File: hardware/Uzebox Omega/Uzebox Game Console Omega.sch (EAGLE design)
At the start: 82 parts, among them CON1 USBSERIALSMD, IC1 MCP1700, IC2 7805T, J1 MICROSD-SWITCH, K1 DC IN, K2 A/V, K5 ISP, K6 RCA-SWMULTICOMP, K7 RCA-SWMULTICOMP, U6 23LC1024

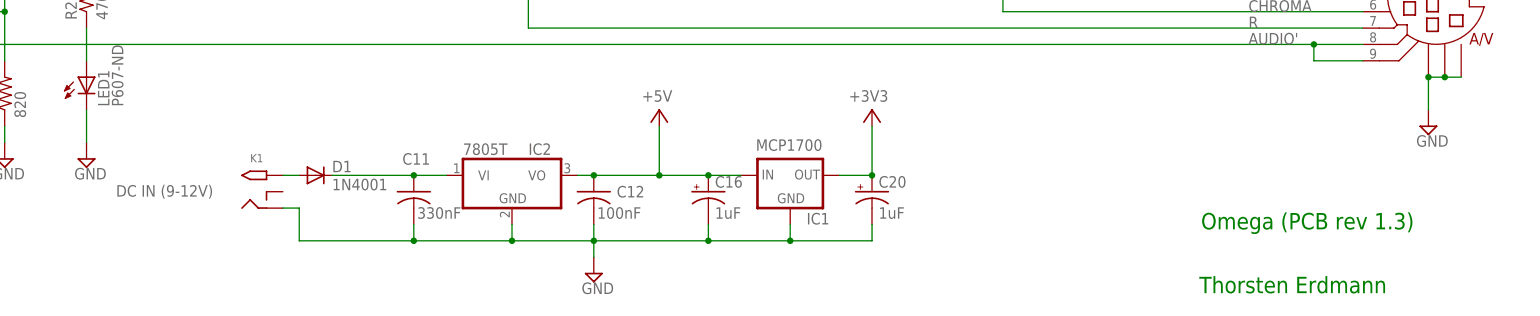
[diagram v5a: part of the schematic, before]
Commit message: Corrected footprint for RCA sockets
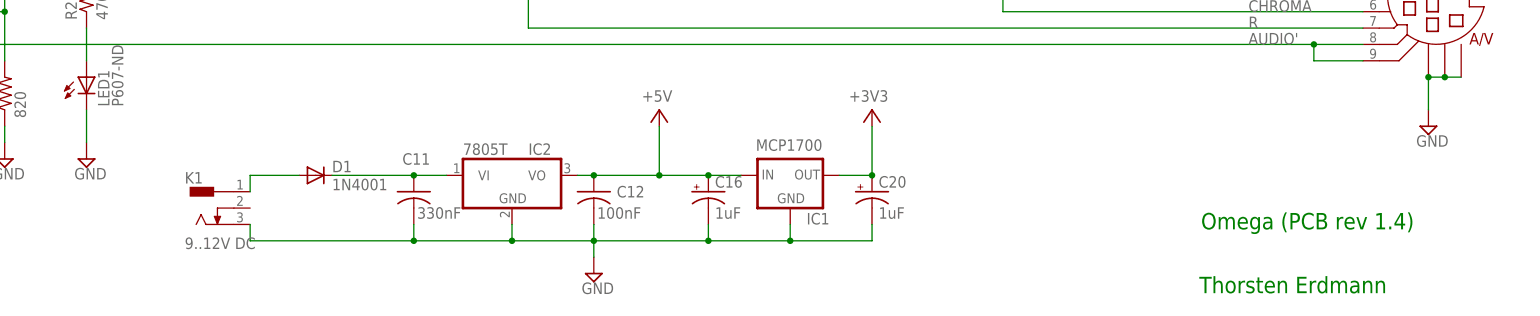
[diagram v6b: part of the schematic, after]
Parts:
- K1: value DC IN -> 9..12V DC; device adafruit:2.1MMJACKTHM -> Thorsten_connectors:DCJACK-SWITCH; LABEL DC IN (9-12V) -> (none)
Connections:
- net GND: now also K1.3; no longer K1.RING
- net N$10: now also K1.1; no longer K1.TIP
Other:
- note added: "Omega (PCB rev 1.4)"
- note removed: "Omega (PCB rev 1.3)"
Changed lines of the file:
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@@
 <part name="SUPPLY12" library="supply2" deviceset="GND" device=""/>
 <part name="R20'" library="resistor" deviceset="R-US_" device="0207/10" value="75"/>
-<part name="K1" library="adafruit" deviceset="2.1MMJACK" device="THM" value="DC IN">
-<attribute name="LABEL" value="DC IN (9-12V)"/>
-</part>
 <part name="D1" library="adafruit" deviceset="1N4004" device="" value="1N4001">
 <attribute name="PN" value="641-1310-1-ND"/>
@@
 <part name="J1" library="Thorsten_diverses" deviceset="MICROSD-SWITCH" device=""/>
 <part name="SUPPLY23" library="supply2" deviceset="GND" device=""/>
+<part name="K1" library="Thorsten_connectors" deviceset="DCJACK-SWITCH" device="" value="9..12V DC"/>
 </parts>
 <sheets>
@@
 <text x="-66.04" y="-33.02" size="1.778" layer="91">along with this work.  If not, see &lt;http://www.gnu.org/licenses/&gt;.</text>
 <text x="-66.04" y="-40.64" size="1.778" layer="91">Video DAC design and SD voltage dividers contributed by Clay Cowgill.</text>
-<text x="254.254" y="-41.402" size="2.54" layer="91">Omega (PCB rev 1.3)</text>
+<text x="254.254" y="-41.402" size="2.54" layer="91">Omega (PCB rev 1.4)</text>
 <text x="165.354" y="145.542" size="1.778" layer="91">Optional Uzenet Interface</text>
 <text x="-66.04" y="-48.26" size="1.778" layer="91">Added Mini-DIN SCART connector and some cleanup by Thorsten Erdmann (Bluescreen@trektech.de)</text>
@@
 <attribute name="VALUE" x="247.65" y="62.738" size="1.778" layer="96"/>
 </instance>
-<instance part="K1" gate="G$1" x="106.68" y="-35.56" smashed="yes">
-<attribute name="NAME" x="106.68" y="-30.988" size="1.27" layer="95"/>
-<attribute name="LABEL" x="85.852" y="-36.322" size="1.778" layer="96"/>
-</instance>
 <instance part="D1" gate="1" x="116.84" y="-33.02" smashed="yes">
 <attribute name="PN" x="116.84" y="-33.02" size="1.778" layer="96" display="off"/>
@@
 <attribute name="VALUE" x="-42.545" y="80.645" size="1.778" layer="96"/>
 </instance>
+<instance part="K1" gate="G$1" x="106.68" y="-38.1"/>
 </instances>
 <busses>
@@
 <wire x1="132.08" y1="-43.18" x2="132.08" y2="-40.64" width="0.1524" layer="91"/>
 <wire x1="132.08" y1="-43.18" x2="147.32" y2="-43.18" width="0.1524" layer="91"/>
-<wire x1="132.08" y1="-43.18" x2="114.3" y2="-43.18" width="0.1524" layer="91"/>
-<wire x1="114.3" y1="-43.18" x2="114.3" y2="-38.1" width="0.1524" layer="91"/>
-<wire x1="114.3" y1="-38.1" x2="111.76" y2="-38.1" width="0.1524" layer="91"/>
+<wire x1="132.08" y1="-43.18" x2="106.68" y2="-43.18" width="0.1524" layer="91"/>
 <wire x1="203.2" y1="-40.64" x2="203.2" y2="-43.18" width="0.1524" layer="91"/>
 <wire x1="203.2" y1="-43.18" x2="190.5" y2="-43.18" width="0.1524" layer="91"/>
@@
 <junction x="147.32" y="-43.18"/>
 <pinref part="SUPPLY15" gate="GND" pin="GND"/>
-<pinref part="K1" gate="G$1" pin="RING"/>
 <pinref part="C11" gate="G$1" pin="2"/>
 <pinref part="C12" gate="G$1" pin="2"/>
@@
 <pinref part="C16" gate="G$1" pin="-"/>
 <pinref part="C20" gate="G$1" pin="-"/>
+<pinref part="K1" gate="G$1" pin="3"/>
+<wire x1="106.68" y1="-40.64" x2="106.68" y2="-43.18" width="0.1524" layer="91"/>
 </segment>
 <segment>
@@
 <net name="N$10" class="0">
 <segment>
-<wire x1="114.3" y1="-33.02" x2="111.76" y2="-33.02" width="0.1524" layer="91"/>
-<pinref part="K1" gate="G$1" pin="TIP"/>
 <pinref part="D1" gate="1" pin="A"/>
-</segment>
-</net>
+<pinref part="K1" gate="G$1" pin="1"/>
+<wire x1="106.68" y1="-35.56" x2="106.68" y2="-33.02" width="0.1524" layer="91"/>
+<wire x1="106.68" y1="-33.02" x2="114.3" y2="-33.02" width="0.1524" layer="91"/>
+</segment>
+</net>
